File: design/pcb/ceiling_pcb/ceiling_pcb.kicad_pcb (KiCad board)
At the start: 2 copper layers, 56 x 200.5 mm, 10 parts, among them J1 Conn_01x09, J10 shock_grid, J2 Conn_01x09, J3 shock_grid, J4 shock_grid, J5 shock_grid, J6 shock_grid, J7 shock_grid, J8 shock_grid, J9 shock_grid

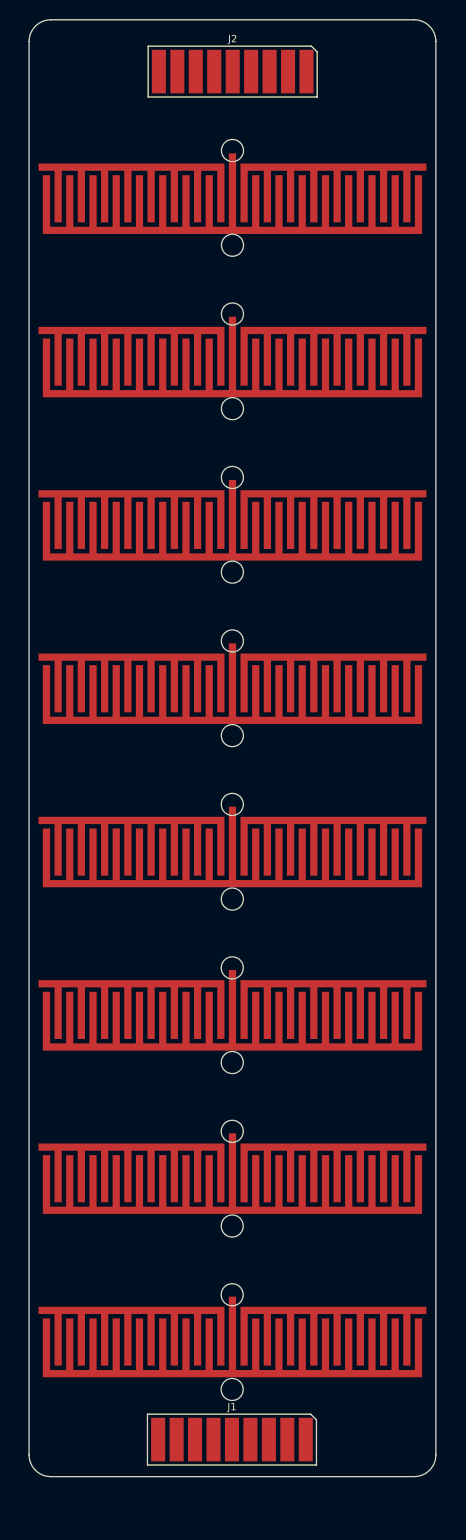
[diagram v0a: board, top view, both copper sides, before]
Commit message: Updated electrode_vertices.py to also generate electrodes interleaved along the long axis, for an orthogonal set of ceiling electrodes. New *_lengthwise footprint should be correct, if not a little wide.
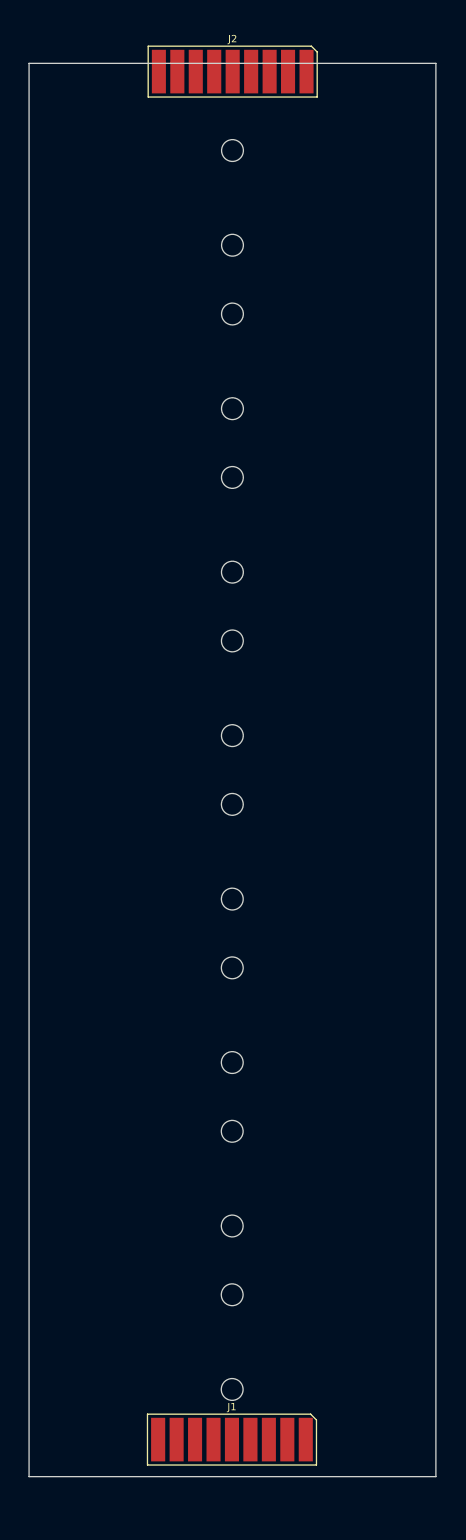
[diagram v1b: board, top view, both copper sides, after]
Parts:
- removed J10, J3, J4, J5, J6, J7, J8, J9: shock_grid, footprints:electrodes_clearance0.6mm
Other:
- board size 56 x 200.5 mm -> 56 x 194.5 mm

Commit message: Fixed bug I made in electrode vertices. Ceiling pcb pretty much done. Need to name F<N> nets consistently across Kicad projects.
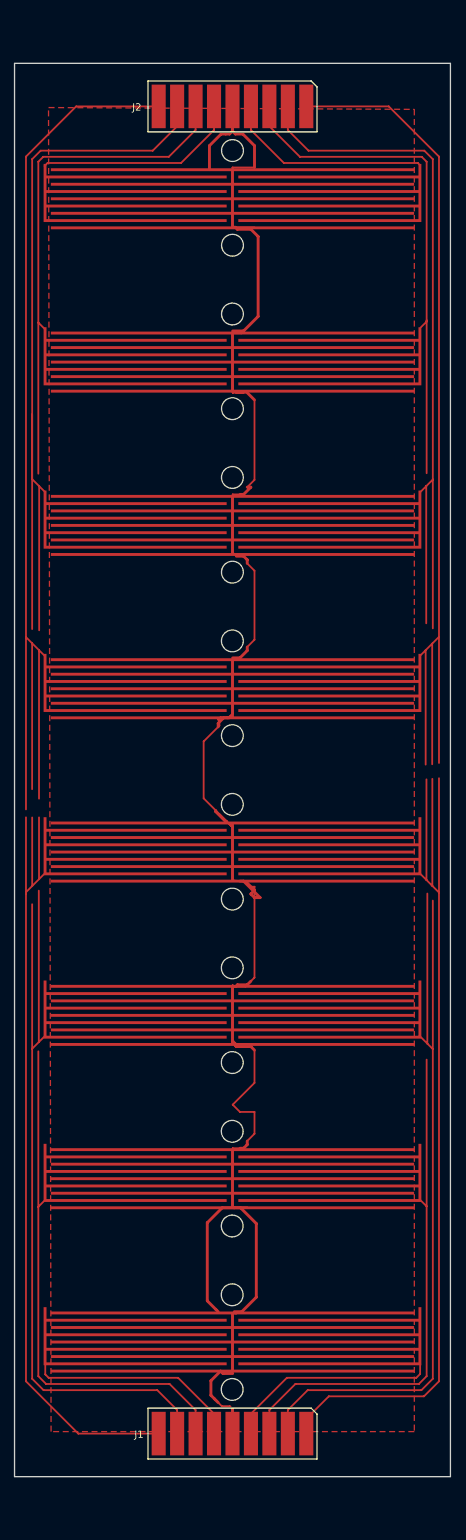
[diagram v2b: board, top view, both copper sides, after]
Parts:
- added J10: shock_grid, footprints:electrodes_clearance0.6mm_W0.4mm_lengthwise, F.Cu at (125.0, 36.4)
- added J3: shock_grid, footprints:electrodes_clearance0.6mm_W0.4mm_lengthwise, F.Cu at (125.0, 193.8)
- added J4: shock_grid, footprints:electrodes_clearance0.6mm_W0.4mm_lengthwise, F.Cu at (125.0, 171.3)
- added J5: shock_grid, footprints:electrodes_clearance0.6mm_W0.4mm_lengthwise, F.Cu at (125.0, 148.8)
- added J6: shock_grid, footprints:electrodes_clearance0.6mm_W0.4mm_lengthwise, F.Cu at (125.0, 126.3)
- added J7: shock_grid, footprints:electrodes_clearance0.6mm_W0.4mm_lengthwise, F.Cu at (125.0, 103.8)
- added J8: shock_grid, footprints:electrodes_clearance0.6mm_W0.4mm_lengthwise, F.Cu at (125.0, 81.3)
- added J9: shock_grid, footprints:electrodes_clearance0.6mm_W0.4mm_lengthwise, F.Cu at (125.0, 58.9)
- moved J2 4.79 mm to (125.0, 23.7)
- moved J1 0.83 mm to (125.0, 206.4)
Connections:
- J2 pad 1: /F16 -> /F10
- J2 pad 2: /F14 -> /F12
- J2 pad 3: /F12 -> /F14
- J2 pad 4: /F10 -> /F16
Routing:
- net /HV: track 0.00 -> 277.0 mm
- net /F9: track 0.00 -> 155.1 mm
- net /F10: track 0.00 -> 140.6 mm
- net /F8: track 0.00 -> 137.8 mm
- net /F7: track 0.00 -> 120.8 mm
- net /F11: track 0.00 -> 120.5 mm
- net /F6: track 0.00 -> 114.1 mm
- net /F5: track 0.00 -> 113.7 mm
- net /F12: track 0.00 -> 110.8 mm
- net /F3: track 0.00 -> 72.9 mm
- net /F4: track 0.00 -> 71.7 mm
- net /F13: track 0.00 -> 71.0 mm
- net /F14: track 0.00 -> 70.6 mm
- net /F1: track 0.00 -> 29.8 mm
- net /F2: track 0.00 -> 29.8 mm
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- added copper zone on F.Cu, net /HV
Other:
- board size 56 x 194.5 mm -> 60 x 194.5 mm

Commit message: Seem to have make_board working to align top and bottom connectors, and J3 on the bottom, but I need to pick different offsets from nearest grid for top and bottom. May need to make ceiling board a little longer on the top. ADD EXTRA MOUNTING HOLES IN BOTTOM.
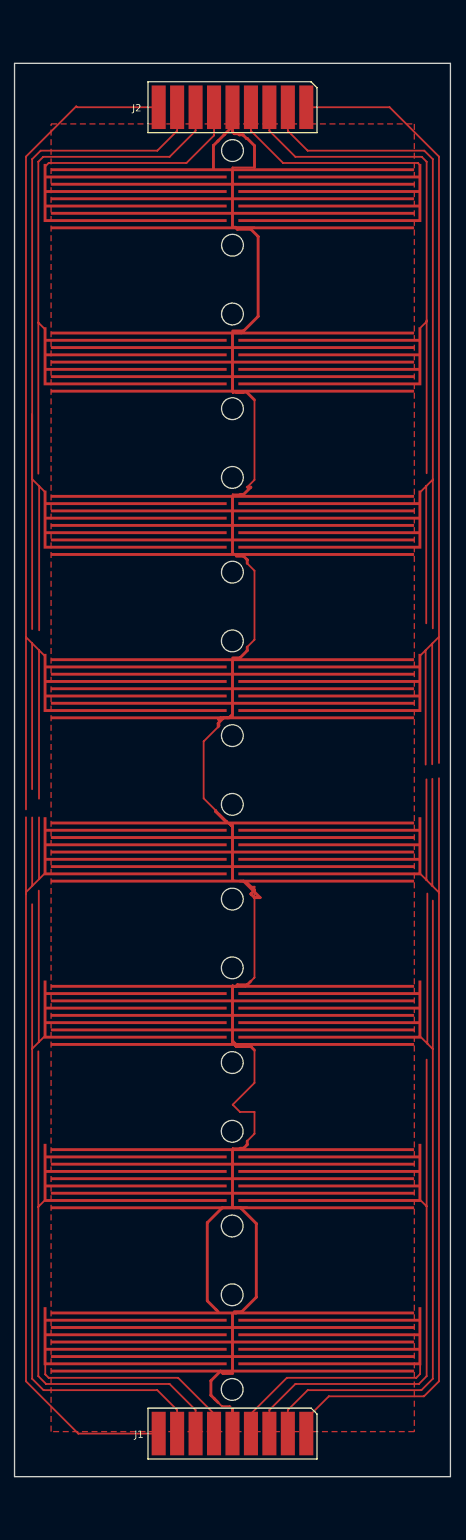
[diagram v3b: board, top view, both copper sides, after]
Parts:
- moved J2 0.12 mm to (125.0, 23.8)
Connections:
- J1 pad 1: /F8 -> /F9
- J1 pad 2: /F6 -> /F11
- J1 pad 3: /F4 -> /F13
- J1 pad 4: /F2 -> /F15
- J1 pad 6: /F1 -> /F16
- J1 pad 7: /F3 -> /F14
- J1 pad 8: /F5 -> /F12
- J1 pad 9: /F7 -> /F10
- J10 pad 1: /F16 -> /F1
- J10 pad 2: /F15 -> /F2
- J2 pad 1: /F10 -> /F7
- J2 pad 2: /F12 -> /F5
- J2 pad 3: /F14 -> /F3
- J2 pad 4: /F16 -> /F1
- J2 pad 6: /F15 -> /F2
- J2 pad 7: /F13 -> /F4
- J2 pad 8: /F11 -> /F6
- J2 pad 9: /F9 -> /F8
- J3 pad 1: /F2 -> /F15
- J3 pad 2: /F1 -> /F16
- J4 pad 1: /F4 -> /F13
- J4 pad 2: /F3 -> /F14
- J5 pad 1: /F6 -> /F11
- J5 pad 2: /F5 -> /F12
- J6 pad 1: /F8 -> /F9
- J6 pad 2: /F7 -> /F10
- J7 pad 1: /F10 -> /F7
- J7 pad 2: /F9 -> /F8
- J8 pad 1: /F12 -> /F5
- J8 pad 2: /F11 -> /F6
- J9 pad 1: /F14 -> /F3
- J9 pad 2: /F13 -> /F4
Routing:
- net /F10: track 140.6 -> 120.8 mm
- net /F7: track 120.8 -> 140.6 mm
- net /F8: track 137.8 -> 155.2 mm
- net /F9: track 155.1 -> 137.8 mm
- net /F6: track 114.1 -> 120.8 mm
- net /F11: track 120.5 -> 114.1 mm
- net /F5: track 113.7 -> 110.8 mm
- net /F12: track 110.8 -> 113.7 mm
- net /HV: track 277.0 -> 279.9 mm
- net /F14: track 70.6 -> 72.9 mm
- net /F3: track 72.9 -> 70.8 mm
- net /F1: track 29.8 -> 28.5 mm
- net /F16: track 28.6 -> 29.8 mm
- net /F15: track 28.6 -> 29.8 mm
- net /F2: track 29.8 -> 28.9 mm
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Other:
- board text added: "TODO how to get zones to extend to polygon F.Cu on same net?"

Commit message: v0.1 boards done. Decided not to add LEDs to shield board for now.
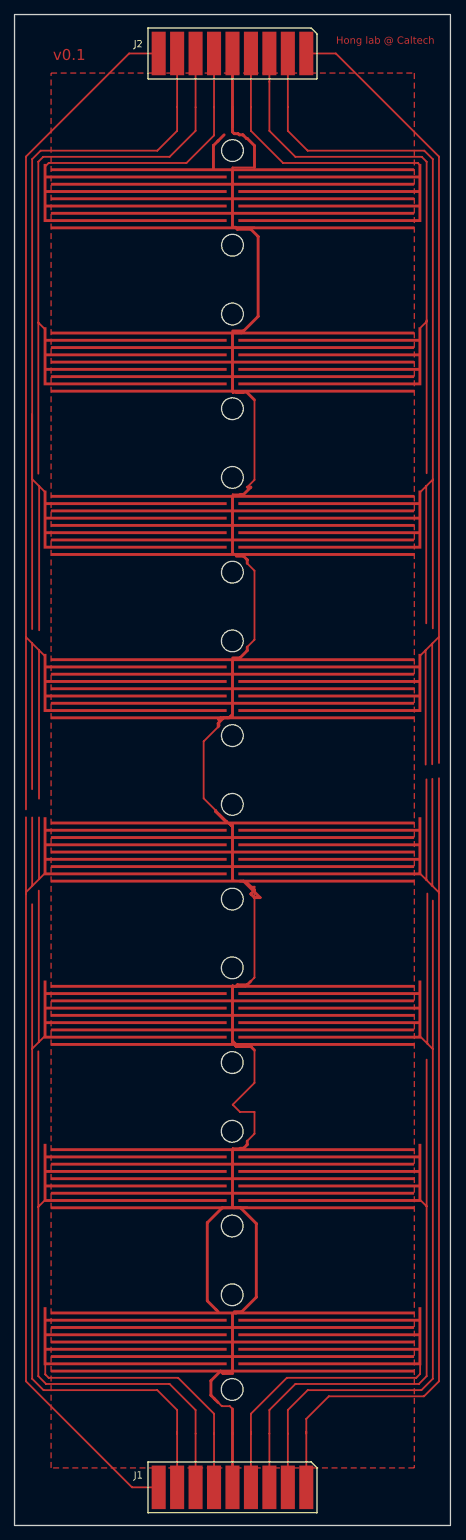
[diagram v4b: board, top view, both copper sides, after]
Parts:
- moved J1 7.40 mm to (125.0, 213.8)
- moved J2 7.40 mm to (125.0, 16.4)
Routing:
- net /HV: track 279.9 -> 292.4 mm
- net /F9: track 137.8 -> 145.5 mm
- net /F12: track 113.7 -> 121.3 mm
- net /F15: track 29.8 -> 37.3 mm
- net /F6: track 120.8 -> 128.2 mm
- net /F5: track 110.8 -> 118.2 mm
- net /F4: track 70.9 -> 78.3 mm
- net /F2: track 28.9 -> 36.3 mm
- net /F1: track 28.5 -> 35.9 mm
- net /F3: track 70.8 -> 78.2 mm
- net /F16: track 29.8 -> 37.2 mm
- net /F14: track 72.9 -> 80.3 mm
- net /F13: track 71.7 -> 79.1 mm
- net /F11: track 114.1 -> 121.5 mm
- net /F7: track 140.6 -> 143.6 mm
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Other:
- board size 60 x 194.5 mm -> 60 x 208 mm
- board text added: "Hong lab @ Caltech"
- board text added: "v0.1"

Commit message: Generated initial gerbers. Going to test against Advanced Circuits system.
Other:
- board text added: "Board should ideally be 1/8" (3.175 mm) thick. Other thicknesses may require different clamps to hold ceiling and all layers tight, such that there are no gaps due to warping. The substrate should be clear, transmitting as much IR light as possible. We used 850 nm IR backlights for some experiments. Since all the conductors in this board are on one side, you should be able to etch it yourself."
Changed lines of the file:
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@@
   (general
     (thickness 1.6)
-    (drawings 23)
+    (drawings 24)
     (tracks 283)
     (zones 0)
@@
     (title "8 chamber shock conditioning ceiling grid")
     (date 06-12-2017)
+    (rev 0.1)
     (company "Hong Lab @ Caltech")
+    (comment 1 github.com/tom-f-oconnell/choice)
   )
   (layers
@@
     (visible_elements FFFFFF7F)
     (pcbplotparams
-      (layerselection 0x00030_ffffffff)
+      (layerselection 0x01000_7fffffff)
       (usegerberextensions false)
       (usegerberattributes true)
@@
       (psnegative false)
       (psa4output false)
-      (plotreference true)
-      (plotvalue true)
+      (plotreference false)
+      (plotvalue false)
       (plotinvisibletext false)
       (padsonsilk false)
@@
       (drillshape 0)
       (scaleselection 1)
-      (outputdirectory ""))
+      (outputdirectory ../gerber/floor_pcb/))
   )
   (net 0 "")
@@
       ))
   )
+  (gr_text "Board should ideally be 1/8\" (3.175 mm) thick.\n\nOther thicknesses may require different clamps\nto hold ceiling and all layers tight, such that there\nare no gaps due to warping.\n\n\n\n\nThe substrate should be clear, transmitting as much\nIR light as possible.  We used 850 nm IR backlights for\nsome experiments.\n\n\n\n\nSince all the conductors in this board are on one side,\nyou should be able to etch it yourself." (at 49.03 53.58) (layer Cmts.User)
+    (effects (font (size 1.5 1.5) (thickness 0.3)))
+  )
   (gr_text v0.1 (at 102.53 16.58) (layer F.Cu)
